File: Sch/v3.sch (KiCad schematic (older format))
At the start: 1 part

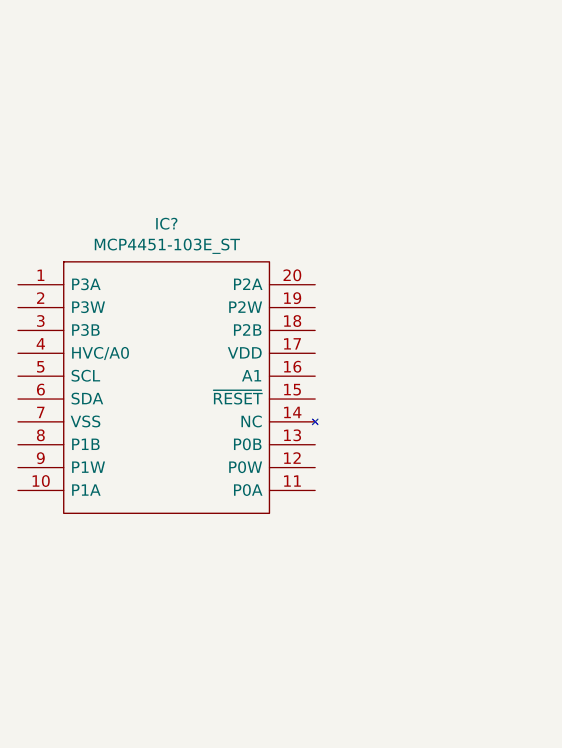
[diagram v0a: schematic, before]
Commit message: Add V3 basic layout
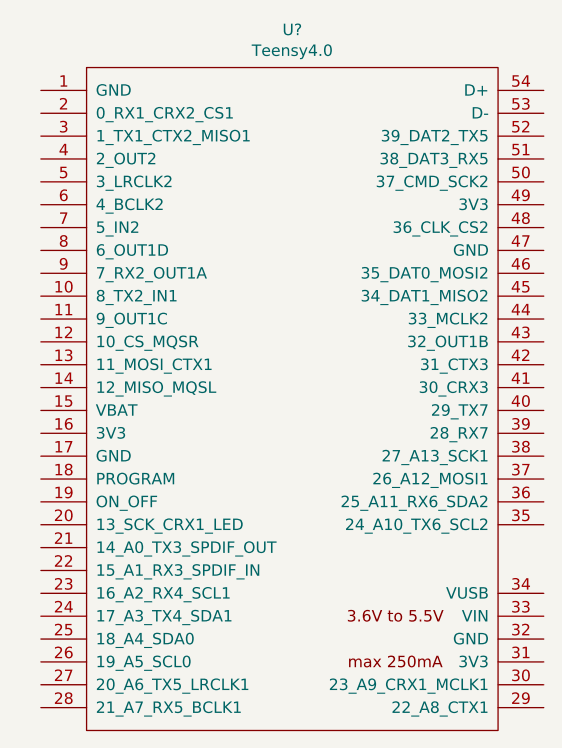
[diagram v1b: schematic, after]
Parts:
- removed IC?: MCP4451-103E_ST, SOP65P640X120-20N, symbol MCP4451-103E_ST:MCP4451-103E_ST
- added U?: Teensy4.0, symbol teensy:Teensy4.0
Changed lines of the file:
@@
 encoding utf-8
 Sheet 1 1
-Title ""
-Date ""
-Rev ""
-Comp ""
-Comment1 ""
+Title "Perception V3"
+Date "2021-05-10"
+Rev "00"
+Comp "Team HART"
+Comment1 "PROTOTYPE"
 Comment2 ""
 Comment3 ""
@@
 $EndDescr
 $Comp
-L MCP4451-103E_ST:MCP4451-103E_ST IC?
-U 1 1 60994818
-P 5000 3350
-F 0 "IC?" H 5650 3615 50  0000 C CNN
-F 1 "MCP4451-103E_ST" H 5650 3524 50  0000 C CNN
-F 2 "SOP65P640X120-20N" H 6150 3450 50  0001 L CNN
-F 3 "http://ww1.microchip.com/downloads/en/DeviceDoc/MCP4451.pdf" H 6150 3350 50  0001 L CNN
-F 4 "MCP4451-103E/ST, Digital Potentiometer 10k 256-Position Linear 2-Channel Serial-SPI 20-Pin TSSOP" H 6150 3250 50  0001 L CNN "Description"
-F 5 "1.2" H 6150 3150 50  0001 L CNN "Height"
-F 6 "Microchip" H 6150 3050 50  0001 L CNN "Manufacturer_Name"
-F 7 "MCP4451-103E/ST" H 6150 2950 50  0001 L CNN "Manufacturer_Part_Number"
-F 8 "579-MCP4451-103E/ST" H 6150 2850 50  0001 L CNN "Mouser Part Number"
-F 9 "https://www.mouser.co.uk/ProductDetail/Microchip-Technology/MCP4451-103E-ST/?qs=opbZS4J%2Fiz2FqmMPXQradQ%3D%3D" H 6150 2750 50  0001 L CNN "Mouser Price/Stock"
-F 10 "MCP4451-103E/ST" H 6150 2650 50  0001 L CNN "Arrow Part Number"
-F 11 "https://www.arrow.com/en/products/mcp4451-103est/microchip-technology" H 6150 2550 50  0001 L CNN "Arrow Price/Stock"
-	1    5000 3350
+L teensy:Teensy4.0 U?
+U 1 1 609956D3
+P 6200 3850
+F 0 "U?" H 6200 5465 50  0000 C CNN
+F 1 "Teensy4.0" H 6200 5374 50  0000 C CNN
+F 2 "" H 5800 4050 50  0001 C CNN
+F 3 "" H 5800 4050 50  0001 C CNN
+	1    6200 3850
 	1    0    0    -1
 $EndComp

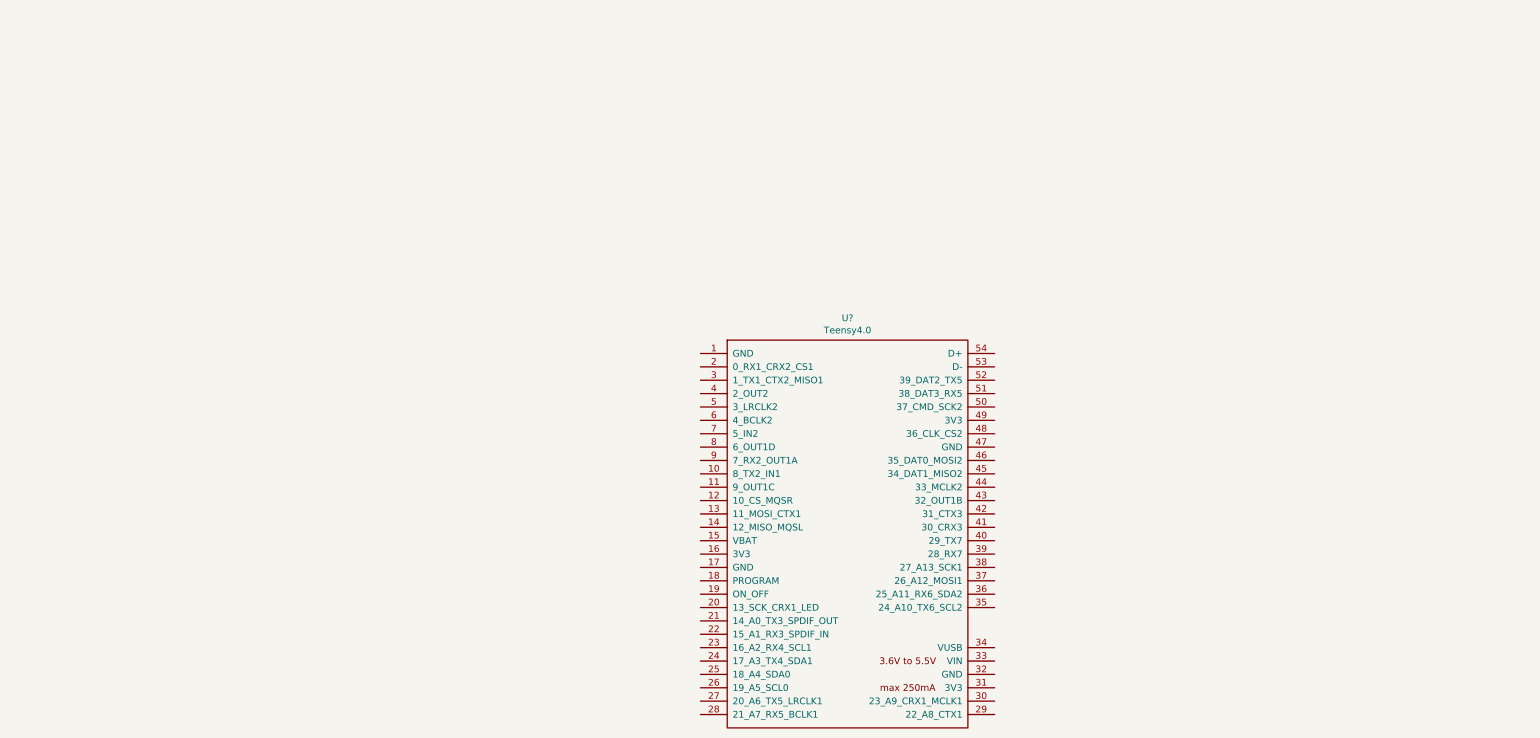
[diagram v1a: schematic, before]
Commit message: First version of first module
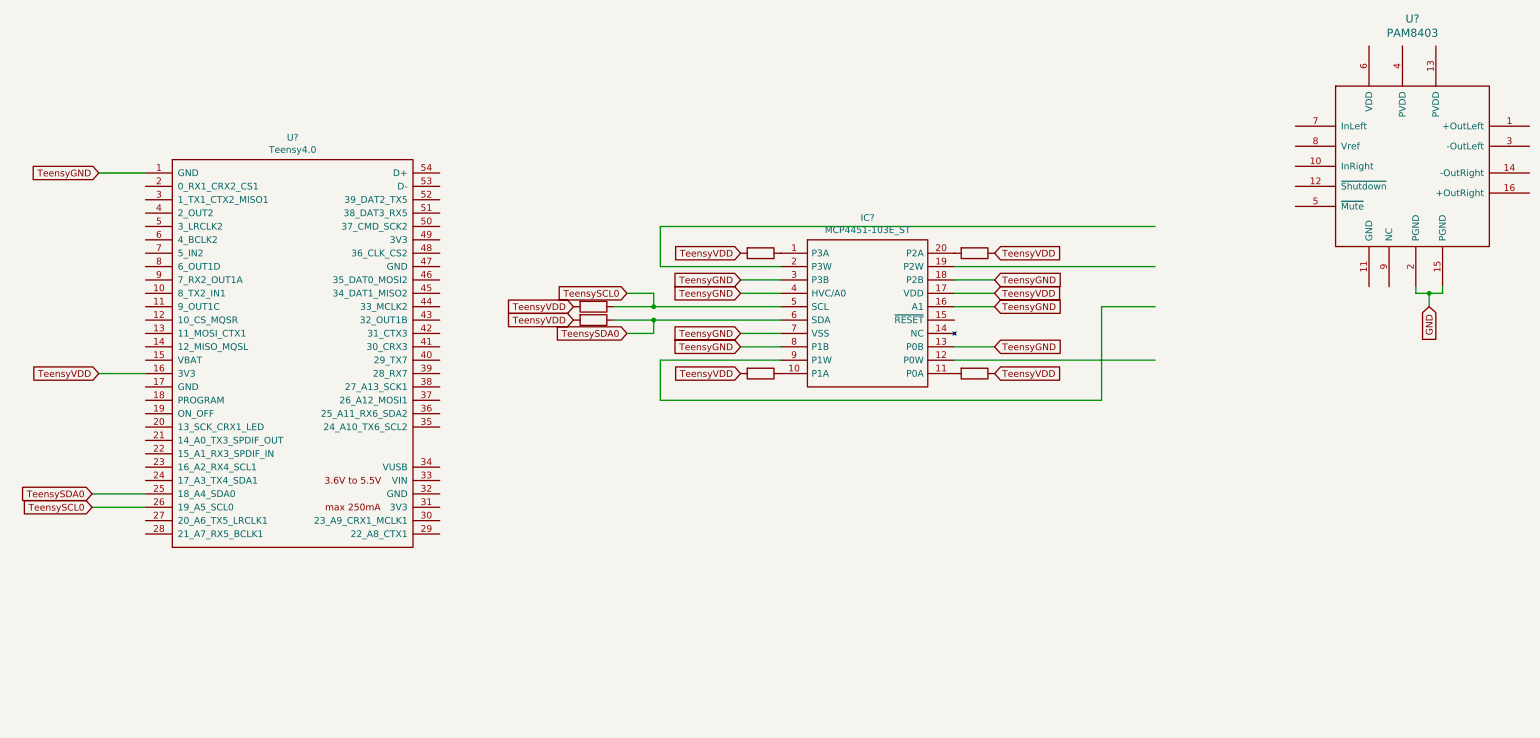
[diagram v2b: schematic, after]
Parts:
- added IC?: MCP4451-103E_ST, SOP65P640X120-20N, symbol MCP4451-103E_ST:MCP4451-103E_ST
- added R? (x2): 3300, symbol Device:R
- added R? (x4): 2000, symbol Device:R
- added U?: PAM8403, symbol pam8403:PAM8403
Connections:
- net labels added: GND, TeensyGND, TeensySCL0, TeensySDA0, TeensyVDD
- wire segments 0 -> 35
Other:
- moved on the sheet: U?
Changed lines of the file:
@@
 L teensy:Teensy4.0 U?
 U 1 1 609956D3
-P 6200 3850
-F 0 "U?" H 6200 5465 50  0000 C CNN
-F 1 "Teensy4.0" H 6200 5374 50  0000 C CNN
-F 2 "" H 5800 4050 50  0001 C CNN
-F 3 "" H 5800 4050 50  0001 C CNN
-	1    6200 3850
+P 2050 2500
+F 0 "U?" H 2050 4115 50  0000 C CNN
+F 1 "Teensy4.0" H 2050 4024 50  0000 C CNN
+F 2 "" H 1650 2700 50  0001 C CNN
+F 3 "" H 1650 2700 50  0001 C CNN
+	1    2050 2500
 	1    0    0    -1
 $EndComp
+Text GLabel 600  1150 0    50   Input ~ 0
+TeensyGND
+Wire Wire Line
+	600  1150 950  1150
+Text GLabel 5400 1950 0    50   Input ~ 0
+TeensyGND
+$Comp
+L MCP4451-103E_ST:MCP4451-103E_ST IC?
+U 1 1 609994CF
+P 5700 1750
+F 0 "IC?" H 6350 2015 50  0000 C CNN
+F 1 "MCP4451-103E_ST" H 6350 1924 50  0000 C CNN
+F 2 "SOP65P640X120-20N" H 6850 1850 50  0001 L CNN
+F 3 "http://ww1.microchip.com/downloads/en/DeviceDoc/MCP4451.pdf" H 6850 1750 50  0001 L CNN
+F 4 "MCP4451-103E/ST, Digital Potentiometer 10k 256-Position Linear 2-Channel Serial-SPI 20-Pin TSSOP" H 6850 1650 50  0001 L CNN "Description"
+F 5 "1.2" H 6850 1550 50  0001 L CNN "Height"
+F 6 "Microchip" H 6850 1450 50  0001 L CNN "Manufacturer_Name"
+F 7 "MCP4451-103E/ST" H 6850 1350 50  0001 L CNN "Manufacturer_Part_Number"
+F 8 "579-MCP4451-103E/ST" H 6850 1250 50  0001 L CNN "Mouser Part Number"
+F 9 "https://www.mouser.co.uk/ProductDetail/Microchip-Technology/MCP4451-103E-ST/?qs=opbZS4J%2Fiz2FqmMPXQradQ%3D%3D" H 6850 1150 50  0001 L CNN "Mouser Price/Stock"
+F 10 "MCP4451-103E/ST" H 6850 1050 50  0001 L CNN "Arrow Part Number"
+F 11 "https://www.arrow.com/en/products/mcp4451-103est/microchip-technology" H 6850 950 50  0001 L CNN "Arrow Price/Stock"
+	1    5700 1750
+	1    0    0    -1
+$EndComp
+Wire Wire Line
+	5400 1950 5700 1950
+Text GLabel 5400 2450 0    50   Input ~ 0
+TeensyGND
+Wire Wire Line
+	5400 2450 5700 2450
+Text GLabel 7300 1950 2    50   Input ~ 0
+TeensyGND
+Wire Wire Line
+	7000 1950 7300 1950
+Text GLabel 7300 2450 2    50   Input ~ 0
+TeensyGND
+Wire Wire Line
+	7000 2450 7300 2450
+Text GLabel 7300 2150 2    50   Input ~ 0
+TeensyGND
+Wire Wire Line
+	7000 2150 7300 2150
+Text GLabel 5400 2350 0    50   Input ~ 0
+TeensyGND
+Wire Wire Line
+	5400 2350 5700 2350
+Text GLabel 5400 2050 0    50   Input ~ 0
+TeensyGND
+Wire Wire Line
+	5400 2050 5700 2050
+Text GLabel 600  2650 0    50   Input ~ 0
+TeensyVDD
+Wire Wire Line
+	600  2650 950  2650
+Text GLabel 5400 2650 0    50   Input ~ 0
+TeensyVDD
+Text GLabel 5400 1750 0    50   Input ~ 0
+TeensyVDD
+Text GLabel 7300 1750 2    50   Input ~ 0
+TeensyVDD
+Text GLabel 7300 2050 2    50   Input ~ 0
+TeensyVDD
+Wire Wire Line
+	7300 2050 7000 2050
+Text GLabel 7300 2650 2    50   Input ~ 0
+TeensyVDD
+Text GLabel 4150 2150 0    50   Input ~ 0
+TeensyVDD
+Text GLabel 4150 2250 0    50   Input ~ 0
+TeensyVDD
+$Comp
+L Device:R R?
+U 1 1 609AA809
+P 4300 2150
+F 0 "R?" V 4093 2150 50  0001 C CNN
+F 1 "3300" V 4184 2150 50  0001 C CNN
+F 2 "" V 4230 2150 50  0001 C CNN
+F 3 "~" H 4300 2150 50  0001 C CNN
+	1    4300 2150
+	0    1    1    0
+$EndComp
+$Comp
+L Device:R R?
+U 1 1 609ABDA5
+P 4300 2250
+F 0 "R?" V 4093 2250 50  0001 C CNN
+F 1 "3300" V 4184 2250 50  0001 C CNN
+F 2 "" V 4230 2250 50  0001 C CNN
+F 3 "~" H 4300 2250 50  0001 C CNN
+	1    4300 2250
+	0    1    1    0
+$EndComp
+Text GLabel 550  3550 0    50   Input ~ 0
+TeensySDA0
+Text GLabel 550  3650 0    50   Input ~ 0
+TeensySCL0
+Wire Wire Line
+	550  3550 950  3550
+Wire Wire Line
+	550  3650 950  3650
+Text GLabel 4550 2050 0    50   Input ~ 0
+TeensySCL0
+Text GLabel 4550 2350 0    50   Input ~ 0
+TeensySDA0
+Wire Wire Line
+	4450 2250 4750 2250
+Wire Wire Line
+	4450 2150 4750 2150
+Wire Wire Line
+	4550 2050 4750 2050
+Wire Wire Line
+	4750 2050 4750 2150
+Connection ~ 4750 2150
+Wire Wire Line
+	4750 2150 5700 2150
+Wire Wire Line
+	4550 2350 4750 2350
+Wire Wire Line
+	4750 2350 4750 2250
+Connection ~ 4750 2250
+Wire Wire Line
+	4750 2250 5700 2250
+$Comp
+L Device:R R?
+U 1 1 609B2344
+P 5550 1750
+F 0 "R?" V 5343 1750 50  0001 C CNN
+F 1 "2000" V 5434 1750 50  0001 C CNN
+F 2 "" V 5480 1750 50  0001 C CNN
+F 3 "~" H 5550 1750 50  0001 C CNN
+	1    5550 1750
+	0    1    1    0
+$EndComp
+$Comp
+L Device:R R?
+U 1 1 609B56EB
+P 5550 2650
+F 0 "R?" V 5343 2650 50  0001 C CNN
+F 1 "2000" V 5434 2650 50  0001 C CNN
+F 2 "" V 5480 2650 50  0001 C CNN
+F 3 "~" H 5550 2650 50  0001 C CNN
+	1    5550 2650
+	0    1    1    0
+$EndComp
+$Comp
+L Device:R R?
+U 1 1 609B60EA
+P 7150 2650
+F 0 "R?" V 6943 2650 50  0001 C CNN
+F 1 "2000" V 7034 2650 50  0001 C CNN
+F 2 "" V 7080 2650 50  0001 C CNN
+F 3 "~" H 7150 2650 50  0001 C CNN
+	1    7150 2650
+	0    1    1    0
+$EndComp
+$Comp
+L Device:R R?
+U 1 1 609B6A02
+P 7150 1750
+F 0 "R?" V 6943 1750 50  0001 C CNN
+F 1 "2000" V 7034 1750 50  0001 C CNN
+F 2 "" V 7080 1750 50  0001 C CNN
+F 3 "~" H 7150 1750 50  0001 C CNN
+	1    7150 1750
+	0    1    1    0
+$EndComp
+Wire Wire Line
+	5700 2550 4800 2550
+Wire Wire Line
+	4800 2550 4800 2850
+Wire Wire Line
+	4800 2850 8100 2850
+Wire Wire Line
+	8100 2150 8500 2150
+Wire Wire Line
+	5700 1850 4800 1850
+Wire Wire Line
+	4800 1850 4800 1550
+Wire Wire Line
+	4800 1550 8500 1550
+Wire Wire Line
+	7000 1850 8500 1850
+Wire Wire Line
+	7000 2550 8500 2550
+Wire Wire Line
+	8100 2150 8100 2850
+$Comp
+L pam8403:PAM8403 U?
+U 1 1 609BDBAE
+P 10350 1050
+F 0 "U?" H 10425 2103 60  0000 C CNN
+F 1 "PAM8403" H 10425 1997 60  0000 C CNN
+F 2 "" H 10350 1050 60  0000 C CNN
+F 3 "" H 10350 1050 60  0000 C CNN
+	1    10350 1050
+	1    0    0    -1
+$EndComp
+Text GLabel 10550 2150 3    50   Input ~ 0
+GND
+Wire Wire Line
+	10650 2000 10650 2050
+Wire Wire Line
+	10650 2050 10550 2050
+Wire Wire Line
+	10550 2050 10550 2150
+Wire Wire Line
+	10450 2000 10450 2050
+Wire Wire Line
+	10450 2050 10550 2050
+Connection ~ 10550 2050
 $EndSCHEMATC

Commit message: Some small changes
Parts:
- added C? (x2): 0.1uF, symbol Device:C
- added C? (x4): 0.47uF, symbol Device:C
- added C? (x6): 1uF, symbol Device:C
- added C? (x2): 470uF, symbol Device:C
- added LS? (x4): Speaker, symbol Device:Speaker
- added R? (x4): 10000, symbol Device:R
- added U?: PAM8403, symbol pam8403:PAM8403
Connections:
- net labels added: PGND, PVDD
- net labels removed: GND
- wire segments 35 -> 93

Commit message: Small optimizations
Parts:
- removed C?: 0.1uF, symbol Device:C
- removed C? (x2): 0.47uF, symbol Device:C
- removed C? (x3): 1uF, symbol Device:C
- removed C?: 470uF, symbol Device:C
- removed LS? (x2): Speaker, symbol Device:Speaker
- removed R? (x2): 10000, symbol Device:R
- removed U?: PAM8403, symbol pam8403:PAM8403
- added C?: 0.1uF, symbol Device:C
- added C? (x2): 0.47uF, symbol Device:C
- added C? (x3): 1uF, symbol Device:C
- added C?: 470uF, symbol Device:C
- added LS? (x2): Speaker, symbol Device:Speaker
- added R? (x2): 10000, symbol Device:R
- added U?: PAM8403, symbol pam8403:PAM8403
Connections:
- net TeensyGND is gone; now on net GNDPWR: C?.1, C?.2, IC?.13 (P0B), IC?.16 (A1), IC?.18 (P2B), IC?.3 (P3B), IC?.4 (HVC/A0), IC?.7 (VSS), IC?.8 (P1B), U?.1 (GND), U?.11 (GND), U?.9 (NC)
- net TeensyVDD: now also C?.2, U?.6 (VDD)
- net PWM22: now reaches U?.29 (22_A8_CTX1)
- net PWM23: now reaches U?.30 (23_A9_CRX1_MCLK1)
- net at IC?.12 (P0W): now also C?.2
- net at IC?.9 (P1W): now also C?.2
- net PGND renamed GNDPWR
- net GNDPWR: now also C?.1, C?.1, C?.1, C?.1, C?.2, U?.11 (GND), U?.15 (PGND), U?.2 (PGND), U?.9 (NC)
- net PVDD renamed +5V
- net +5V: now also C?.2, C?.2, C?.2, U?.13 (PVDD), U?.4 (PVDD)
- new net: LS?.1, U?.1 (+OutLeft)
- new net: R?.1, U?.10 (InRight)
- new net: LS?.1, U?.14 (-OutRight)
- new net: LS?.2, U?.16 (+OutRight)
- new net: LS?.2, U?.3 (-OutLeft)
- new net: R?.1, U?.7 (InLeft)
- new net: C?.1, U?.8 (Vref)
- new net: C?.1, R?.2 (x2)

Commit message: Added all different pots and amps and connected them to the correct frequency pins
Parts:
- added C? (x10): 0.1uF, symbol Device:C
- added C? (x20): 0.47uF, symbol Device:C
- added C? (x30): 1uF, symbol Device:C
- added C? (x10): 470uF, symbol Device:C
- added IC? (x5): MCP4451-103E_ST, SOP65P640X120-20N, symbol MCP4451-103E_ST:MCP4451-103E_ST
- added LS? (x20): Speaker, symbol Device:Speaker
- added R? (x10): 2200, symbol Device:R
- added R? (x20): 51000, symbol Device:R
- added R? (x20): 10000, symbol Device:R
- added U? (x10): PAM8403, symbol pam8403:PAM8403
- R? (x2): value 3300 -> 2200
- R? (x4): value 2000 -> 51000
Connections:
- net +5V: now also C?.2, C?.2, C?.2, C?.2, C?.2, C?.2, C?.2, C?.2, C?.2, C?.2, C?.2, C?.2, C?.2, C?.2, C?.2, C?.2, C?.2, C?.2, C?.2, C?.2, C?.2, C?.2, C?.2, C?.2, C?.2, C?.2, C?.2, C?.2, C?.2, C?.2, U?.13 (PVDD), U?.13 (PVDD), U?.13 (PVDD), U?.13 (PVDD), U?.13 (PVDD), U?.13 (PVDD), U?.13 (PVDD), U?.13 (PVDD), U?.13 (PVDD), U?.13 (PVDD), U?.4 (PVDD), U?.4 (PVDD), U?.4 (PVDD), U?.4 (PVDD), U?.4 (PVDD), U?.4 (PVDD), U?.4 (PVDD), U?.4 (PVDD), U?.4 (PVDD), U?.4 (PVDD)
- net GNDPWR: now also C?.1, C?.1, C?.1, C?.1, C?.1, C?.1, C?.1, C?.1, C?.1, C?.1, C?.1, C?.1, C?.1, C?.1, C?.1, C?.1, C?.1, C?.1, C?.1, C?.1, C?.1, C?.1, C?.1, C?.1, C?.1, C?.1, C?.1, C?.1, C?.1, C?.1, C?.1, C?.1, C?.1, C?.1, C?.1, C?.1, C?.1, C?.1, C?.1, C?.1, C?.2, C?.2, C?.2, C?.2, C?.2, C?.2, C?.2, C?.2, C?.2, C?.2, IC?.13 (P0B), IC?.13 (P0B), IC?.13 (P0B), IC?.13 (P0B), IC?.13 (P0B), IC?.16 (A1), IC?.16 (A1), IC?.16 (A1), IC?.16 (A1), IC?.16 (A1), IC?.18 (P2B), IC?.18 (P2B), IC?.18 (P2B), IC?.18 (P2B), IC?.18 (P2B), IC?.3 (P3B), IC?.3 (P3B), IC?.3 (P3B), IC?.3 (P3B), IC?.3 (P3B), IC?.4 (HVC/A0), IC?.4 (HVC/A0), IC?.4 (HVC/A0), IC?.4 (HVC/A0), IC?.4 (HVC/A0), IC?.7 (VSS), IC?.7 (VSS), IC?.7 (VSS), IC?.7 (VSS), IC?.7 (VSS), IC?.8 (P1B), IC?.8 (P1B), IC?.8 (P1B), IC?.8 (P1B), IC?.8 (P1B), U?.11 (GND), U?.11 (GND), U?.11 (GND), U?.11 (GND), U?.11 (GND), U?.11 (GND), U?.11 (GND), U?.11 (GND), U?.11 (GND), U?.11 (GND), U?.15 (PGND), U?.15 (PGND), U?.15 (PGND), U?.15 (PGND), U?.15 (PGND), U?.15 (PGND), U?.15 (PGND), U?.15 (PGND), U?.15 (PGND), U?.15 (PGND), U?.2 (PGND), U?.2 (PGND), U?.2 (PGND), U?.2 (PGND), U?.2 (PGND), U?.2 (PGND), U?.2 (PGND), U?.2 (PGND), U?.2 (PGND), U?.2 (PGND), U?.9 (NC), U?.9 (NC), U?.9 (NC), U?.9 (NC), U?.9 (NC), U?.9 (NC), U?.9 (NC), U?.9 (NC), U?.9 (NC), U?.9 (NC)
- net TeensySCL0: now also IC?.5 (SCL), IC?.5 (SCL), IC?.5 (SCL), R?.1, R?.1, R?.1
- net TeensySDA0: now also IC?.6 (SDA), IC?.6 (SDA), IC?.6 (SDA), R?.1, R?.1, R?.1
- net TeensyVDD: now also C?.2, C?.2, C?.2, C?.2, C?.2, C?.2, C?.2, C?.2, C?.2, C?.2, IC?.17 (VDD), IC?.17 (VDD), IC?.17 (VDD), IC?.17 (VDD), IC?.17 (VDD), R?.2, R?.2, R?.2, R?.2, R?.2, R?.2, R?.2, R?.2, R?.2, R?.2, U?.6 (VDD), U?.6 (VDD), U?.6 (VDD), U?.6 (VDD), U?.6 (VDD), U?.6 (VDD), U?.6 (VDD), U?.6 (VDD), U?.6 (VDD), U?.6 (VDD); no longer R?.1, R?.1, R?.2, R?.2
- net Freq6: now reaches U?.12 (10_CS_MQSR)
- net Freq6: now also R?.2
- net Freq7: now reaches U?.13 (11_MOSI_CTX1)
- net Freq7: now also R?.1
- net Freq8: now reaches U?.14 (12_MISO_MQSL)
- net Freq8: now also R?.2
- net Freq9: now reaches U?.20 (13_SCK_CRX1_LED)
- net Freq9: now also R?.1, R?.2
- net Freq10: now reaches U?.21 (14_A0_TX3_SPDIF_OUT)
- net Freq10: now also R?.1, R?.2
- net Freq11: now reaches U?.22 (15_A1_RX3_SPDIF_IN)
- net Freq11: now also R?.1, R?.2
- net TeensySCL1: now reaches U?.23 (16_A2_RX4_SCL1)
- net TeensySCL1: now also IC?.5 (SCL), IC?.5 (SCL), R?.1, R?.1
- net TeensySDA1: now reaches U?.24 (17_A3_TX4_SDA1)
- net TeensySDA1: now also IC?.6 (SDA), IC?.6 (SDA), R?.1, R?.1
- net Freq13: now reaches U?.39 (28_RX7)
- net Freq13: now also R?.1, R?.2
- net Freq1: now reaches U?.4 (2_OUT2)
- net Freq1: now also R?.1
- net Freq14: now reaches U?.45 (34_DAT1_MISO2)
- net Freq14: now also R?.1, R?.2
- net Freq15: now reaches U?.48 (36_CLK_CS2)
- net Freq15: now also R?.1, R?.2
- net Freq16: now reaches U?.50 (37_CMD_SCK2)
- net Freq16: now also R?.1, R?.2
- net Freq2: now reaches U?.6 (4_BCLK2)
- net Freq2: now also R?.2
- net Freq3: now reaches U?.7 (5_IN2)
- net Freq3: now also R?.1
- net Freq4: now reaches U?.8 (6_OUT1D)
- net Freq4: now also R?.2
- net Freq5: now reaches U?.9 (7_RX2_OUT1A)
- net Freq5: now also R?.1
- net PWM22 renamed Freq12
- net Freq12: now also R?.1, R?.2
- net PWM23: no longer names the net of U?.30 (23_A9_CRX1_MCLK1)
- new net: IC?.1 (P3A), R?.1 (x5)
- new net: IC?.10 (P1A), R?.1 (x5)
- new net: IC?.11 (P0A), R?.2 (x5)
- new net: C?.2, IC?.12 (P0W) (x5)
- new net: C?.2, IC?.19 (P2W) (x5)
- new net: C?.2, IC?.2 (P3W) (x5)
- new net: IC?.20 (P2A), R?.2 (x5)
- new net: C?.2, IC?.9 (P1W) (x4)
- new net: LS?.1, U?.1 (+OutLeft) (x10)
- new net: R?.1, U?.10 (InRight) (x10)
- new net: LS?.1, U?.14 (-OutRight) (x10)
- new net: LS?.2, U?.16 (+OutRight) (x10)
- new net: LS?.2, U?.3 (-OutLeft) (x10)
- new net: R?.1, U?.7 (InLeft) (x10)
- new net: C?.1, U?.8 (Vref) (x10)
- new net: C?.1, R?.2 (x20)
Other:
- moved on the sheet: LS?
